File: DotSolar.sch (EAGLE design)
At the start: 19 parts, among them IC2 SI1145, Q1 BSH203, U1 ISL29125

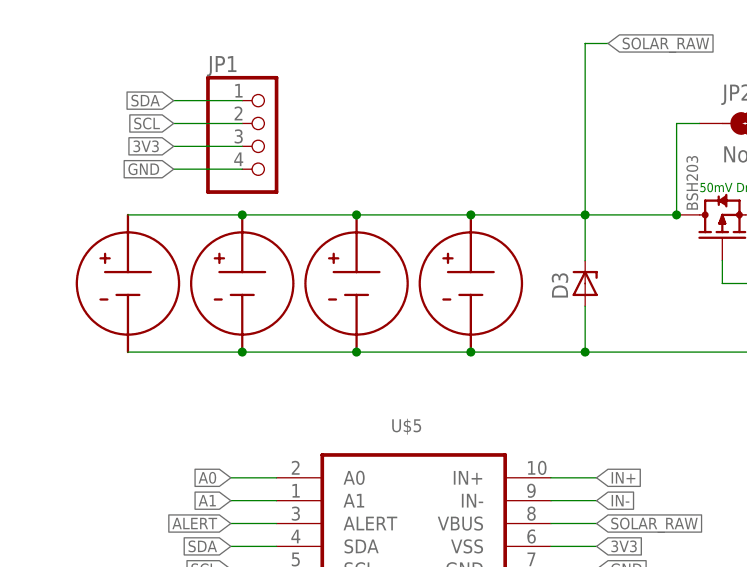
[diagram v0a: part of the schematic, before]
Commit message: Update with exdended solar pad design
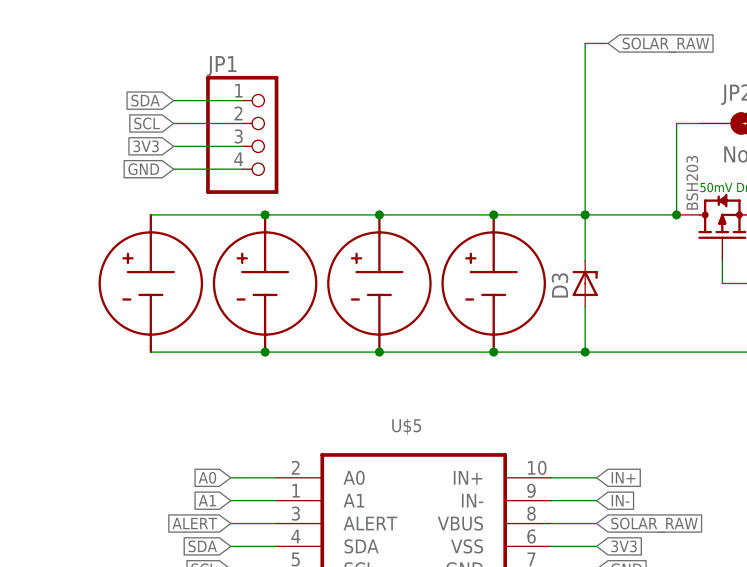
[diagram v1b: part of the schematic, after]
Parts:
- removed U$4: KXOB22-01X8F, IXYS_Solar_cells:KXOB22-01X8F
- added U$6: KXOB22-01X8F_EXTENDED_PADS, IXYS_Solar_cells:KXOB22-01X8F_EXTENDED_PADS
- U$1, U$2, U$3: value KXOB22-01X8F -> KXOB22-01X8F_EXTENDED_PADS; device IXYS_Solar_cells:KXOB22-01X8F -> IXYS_Solar_cells:KXOB22-01X8F_EXTENDED_PADS
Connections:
- net GND: now also U$6.P$1; no longer U$4.P$1
- net SOLAR_RAW: now also U$6.P$2; no longer U$4.P$2
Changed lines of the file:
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@@
 <parts>
 <part name="LOGO1" library="Particle-Devices" deviceset="OSHW-LOGO" device="S"/>
-<part name="U$1" library="IXYS_Solar_cells" deviceset="KXOB22-01X8F" device=""/>
-<part name="U$2" library="IXYS_Solar_cells" deviceset="KXOB22-01X8F" device=""/>
-<part name="U$3" library="IXYS_Solar_cells" deviceset="KXOB22-01X8F" device=""/>
-<part name="U$4" library="IXYS_Solar_cells" deviceset="KXOB22-01X8F" device=""/>
 <part name="SJ2" library="SparkFun" deviceset="SOLDERJUMPER_2WAY" device="PASTE2&amp;3"/>
 <part name="SJ3" library="SparkFun" deviceset="SOLDERJUMPER_2WAY" device="PASTE2&amp;3"/>
@@
 <part name="D1" library="PP_Passives" deviceset="DIODE" device="_B130-13-F"/>
 <part name="JP2" library="SparkFun-Jumpers" deviceset="JUMPER-SMT_2_NO" device="_SILK" value="NoBattery, only Capacitor"/>
+<part name="U$6" library="IXYS_Solar_cells" deviceset="KXOB22-01X8F_EXTENDED_PADS" device=""/>
+<part name="U$1" library="IXYS_Solar_cells" deviceset="KXOB22-01X8F_EXTENDED_PADS" device=""/>
+<part name="U$2" library="IXYS_Solar_cells" deviceset="KXOB22-01X8F_EXTENDED_PADS" device=""/>
+<part name="U$3" library="IXYS_Solar_cells" deviceset="KXOB22-01X8F_EXTENDED_PADS" device=""/>
 </parts>
 <sheets>
@@
 <instances>
 <instance part="LOGO1" gate="G$1" x="27.94" y="96.52"/>
-<instance part="U$1" gate="G$1" x="22.86" y="55.88"/>
-<instance part="U$2" gate="G$1" x="35.56" y="55.88"/>
-<instance part="U$3" gate="G$1" x="48.26" y="55.88"/>
-<instance part="U$4" gate="G$1" x="60.96" y="55.88"/>
 <instance part="SJ2" gate="G$1" x="22.86" y="-10.16" rot="R180"/>
 <instance part="SJ3" gate="G$1" x="53.34" y="-10.16" rot="R180"/>
@@
 <instance part="D1" gate="G$1" x="96.52" y="63.5"/>
 <instance part="JP2" gate="G$1" x="91.44" y="73.66"/>
+<instance part="U$6" gate="G$1" x="25.4" y="55.88"/>
+<instance part="U$1" gate="G$1" x="38.1" y="55.88"/>
+<instance part="U$2" gate="G$1" x="50.8" y="55.88"/>
+<instance part="U$3" gate="G$1" x="63.5" y="55.88"/>
 </instances>
 <busses>
@@
 <net name="SOLAR_RAW" class="0">
 <segment>
+<pinref part="U$5" gate="G$1" pin="VBUS"/>
+<wire x1="69.85" y1="29.21" x2="74.93" y2="29.21" width="0.1524" layer="91"/>
+<label x="74.93" y="29.21" size="1.27" layer="95" xref="yes"/>
+</segment>
+<segment>
 <wire x1="73.66" y1="58.42" x2="73.66" y2="63.5" width="0.1524" layer="91"/>
-<wire x1="73.66" y1="63.5" x2="60.96" y2="63.5" width="0.1524" layer="91"/>
-<wire x1="60.96" y1="63.5" x2="48.26" y2="63.5" width="0.1524" layer="91"/>
-<wire x1="48.26" y1="63.5" x2="35.56" y2="63.5" width="0.1524" layer="91"/>
-<wire x1="35.56" y1="63.5" x2="22.86" y2="63.5" width="0.1524" layer="91"/>
+<wire x1="73.66" y1="63.5" x2="63.5" y2="63.5" width="0.1524" layer="91"/>
 <junction x="73.66" y="63.5"/>
+<wire x1="63.5" y1="63.5" x2="50.8" y2="63.5" width="0.1524" layer="91"/>
+<wire x1="50.8" y1="63.5" x2="38.1" y2="63.5" width="0.1524" layer="91"/>
+<wire x1="38.1" y1="63.5" x2="25.4" y2="63.5" width="0.1524" layer="91"/>
 <wire x1="83.82" y1="63.5" x2="73.66" y2="63.5" width="0.1524" layer="91"/>
-<pinref part="U$1" gate="G$1" pin="P$2"/>
-<pinref part="U$2" gate="G$1" pin="P$2"/>
-<junction x="35.56" y="63.5"/>
-<pinref part="U$3" gate="G$1" pin="P$2"/>
-<junction x="48.26" y="63.5"/>
-<pinref part="U$4" gate="G$1" pin="P$2"/>
-<junction x="60.96" y="63.5"/>
 <pinref part="D3" gate="G$1" pin="C"/>
 <pinref part="Q1" gate="Q" pin="D"/>
@@
 <wire x1="83.82" y1="73.66" x2="83.82" y2="63.5" width="0.1524" layer="91"/>
 <junction x="83.82" y="63.5"/>
-</segment>
-<segment>
-<pinref part="U$5" gate="G$1" pin="VBUS"/>
-<wire x1="69.85" y1="29.21" x2="74.93" y2="29.21" width="0.1524" layer="91"/>
-<label x="74.93" y="29.21" size="1.27" layer="95" xref="yes"/>
+<pinref part="U$6" gate="G$1" pin="P$2"/>
+<pinref part="U$1" gate="G$1" pin="P$2"/>
+<junction x="38.1" y="63.5"/>
+<pinref part="U$2" gate="G$1" pin="P$2"/>
+<junction x="50.8" y="63.5"/>
+<pinref part="U$3" gate="G$1" pin="P$2"/>
+<junction x="63.5" y="63.5"/>
 </segment>
 </net>
@@
 <label x="27.94" y="68.58" size="1.27" layer="95" rot="R180" xref="yes"/>
 <pinref part="JP1" gate="A" pin="4"/>
-</segment>
-<segment>
-<wire x1="73.66" y1="53.34" x2="73.66" y2="48.26" width="0.1524" layer="91"/>
-<wire x1="22.86" y1="48.26" x2="35.56" y2="48.26" width="0.1524" layer="91"/>
-<wire x1="35.56" y1="48.26" x2="48.26" y2="48.26" width="0.1524" layer="91"/>
-<wire x1="48.26" y1="48.26" x2="60.96" y2="48.26" width="0.1524" layer="91"/>
-<wire x1="60.96" y1="48.26" x2="73.66" y2="48.26" width="0.1524" layer="91"/>
-<wire x1="73.66" y1="48.26" x2="102.87" y2="48.26" width="0.1524" layer="91"/>
-<junction x="73.66" y="48.26"/>
-<label x="102.87" y="48.26" size="1.27" layer="95" xref="yes"/>
-<pinref part="U$1" gate="G$1" pin="P$1"/>
-<pinref part="U$2" gate="G$1" pin="P$1"/>
-<junction x="35.56" y="48.26"/>
-<pinref part="U$3" gate="G$1" pin="P$1"/>
-<junction x="48.26" y="48.26"/>
-<pinref part="U$4" gate="G$1" pin="P$1"/>
-<junction x="60.96" y="48.26"/>
-<pinref part="D3" gate="G$1" pin="A"/>
 </segment>
 <segment>
@@
 <label x="74.93" y="24.13" size="1.27" layer="95" xref="yes"/>
 </segment>
+<segment>
+<wire x1="73.66" y1="53.34" x2="73.66" y2="48.26" width="0.1524" layer="91"/>
+<wire x1="25.4" y1="48.26" x2="38.1" y2="48.26" width="0.1524" layer="91"/>
+<wire x1="38.1" y1="48.26" x2="50.8" y2="48.26" width="0.1524" layer="91"/>
+<wire x1="50.8" y1="48.26" x2="63.5" y2="48.26" width="0.1524" layer="91"/>
+<wire x1="63.5" y1="48.26" x2="73.66" y2="48.26" width="0.1524" layer="91"/>
+<wire x1="73.66" y1="48.26" x2="102.87" y2="48.26" width="0.1524" layer="91"/>
+<junction x="73.66" y="48.26"/>
+<label x="102.87" y="48.26" size="1.27" layer="95" xref="yes"/>
+<pinref part="D3" gate="G$1" pin="A"/>
+<pinref part="U$6" gate="G$1" pin="P$1"/>
+<pinref part="U$1" gate="G$1" pin="P$1"/>
+<junction x="38.1" y="48.26"/>
+<pinref part="U$2" gate="G$1" pin="P$1"/>
+<junction x="50.8" y="48.26"/>
+<pinref part="U$3" gate="G$1" pin="P$1"/>
+<junction x="63.5" y="48.26"/>
+</segment>
 </net>

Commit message: Add C1(10uF) and C2(1uF)
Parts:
- added C1: 10uF, rcl:C-EUC0603
- added C2: 0.1uF, rcl:C-EUC0603
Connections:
- net 3V3: now also C1.1, C2.1
- net GND: now also C1.2, C2.2
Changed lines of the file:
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@@
 <part name="U$2" library="IXYS_Solar_cells" deviceset="KXOB22-01X8F_EXTENDED_PADS" device=""/>
 <part name="U$3" library="IXYS_Solar_cells" deviceset="KXOB22-01X8F_EXTENDED_PADS" device=""/>
+<part name="C1" library="rcl" deviceset="C-EU" device="C0603" value="10uF"/>
+<part name="C2" library="rcl" deviceset="C-EU" device="C0603" value="0.1uF"/>
 </parts>
 <sheets>
@@
 <instance part="U$2" gate="G$1" x="50.8" y="55.88"/>
 <instance part="U$3" gate="G$1" x="63.5" y="55.88"/>
+<instance part="C1" gate="G$1" x="200.66" y="63.5"/>
+<instance part="C2" gate="G$1" x="210.82" y="63.5"/>
 </instances>
 <busses>
@@
 <junction x="63.5" y="48.26"/>
 </segment>
+<segment>
+<pinref part="C1" gate="G$1" pin="2"/>
+<pinref part="C2" gate="G$1" pin="2"/>
+<wire x1="200.66" y1="58.42" x2="205.74" y2="58.42" width="0.1524" layer="91"/>
+<wire x1="205.74" y1="58.42" x2="210.82" y2="58.42" width="0.1524" layer="91"/>
+<junction x="205.74" y="58.42"/>
+<wire x1="205.74" y1="58.42" x2="205.74" y2="53.34" width="0.1524" layer="91"/>
+<label x="205.74" y="53.34" size="1.27" layer="95" xref="yes"/>
+</segment>
 </net>
 <net name="3V3" class="0">
@@
 <junction x="99.06" y="63.5"/>
 </segment>
+<segment>
+<pinref part="C2" gate="G$1" pin="1"/>
+<pinref part="C1" gate="G$1" pin="1"/>
+<wire x1="210.82" y1="66.04" x2="205.74" y2="66.04" width="0.1524" layer="91"/>
+<wire x1="205.74" y1="66.04" x2="200.66" y2="66.04" width="0.1524" layer="91"/>
+<wire x1="205.74" y1="66.04" x2="205.74" y2="71.12" width="0.1524" layer="91"/>
+<junction x="205.74" y="66.04"/>
+<label x="205.74" y="71.12" size="1.27" layer="95" xref="yes"/>
+</segment>
 </net>

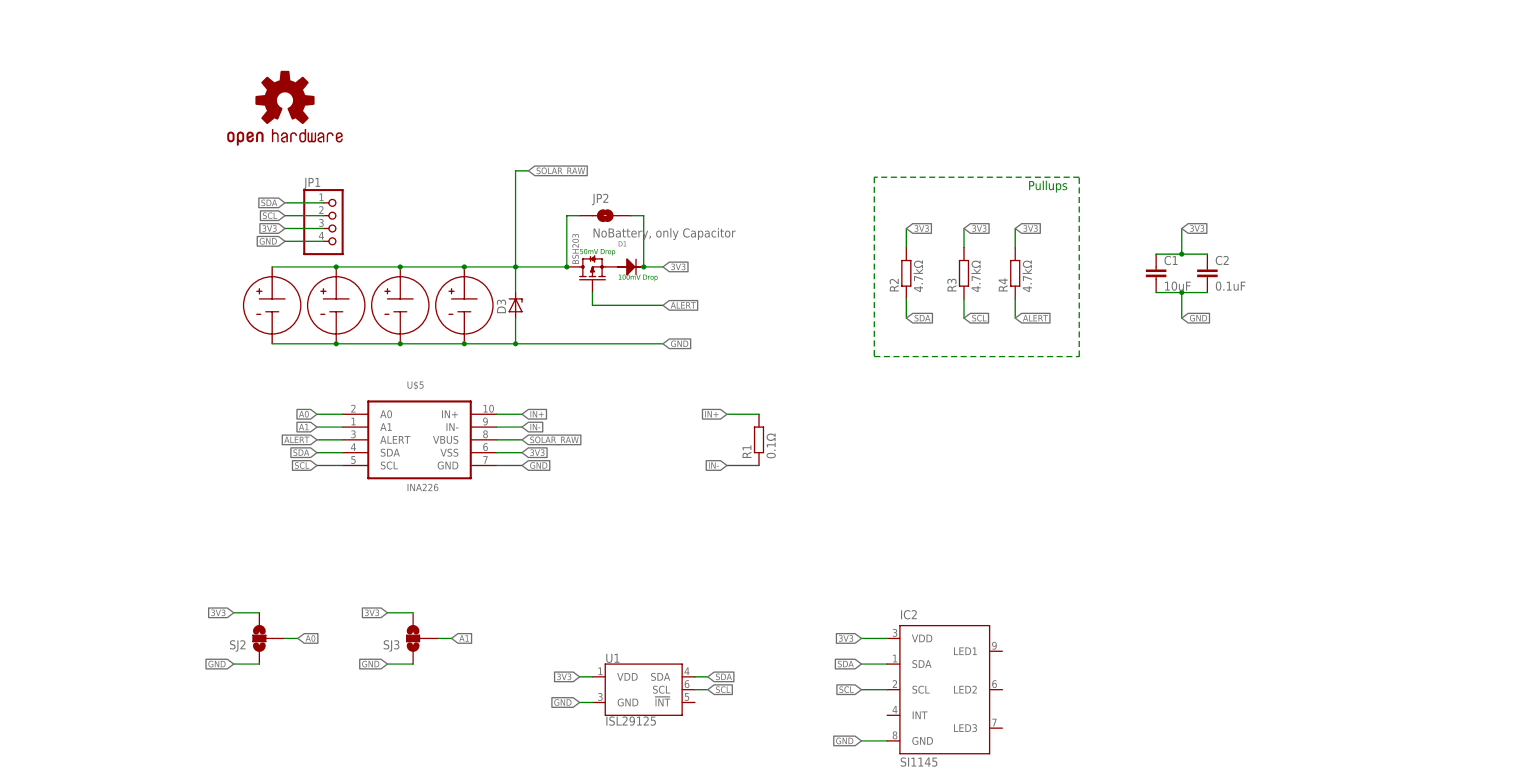
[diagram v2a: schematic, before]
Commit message: Add CAT24M01 8Mbit EEPROM
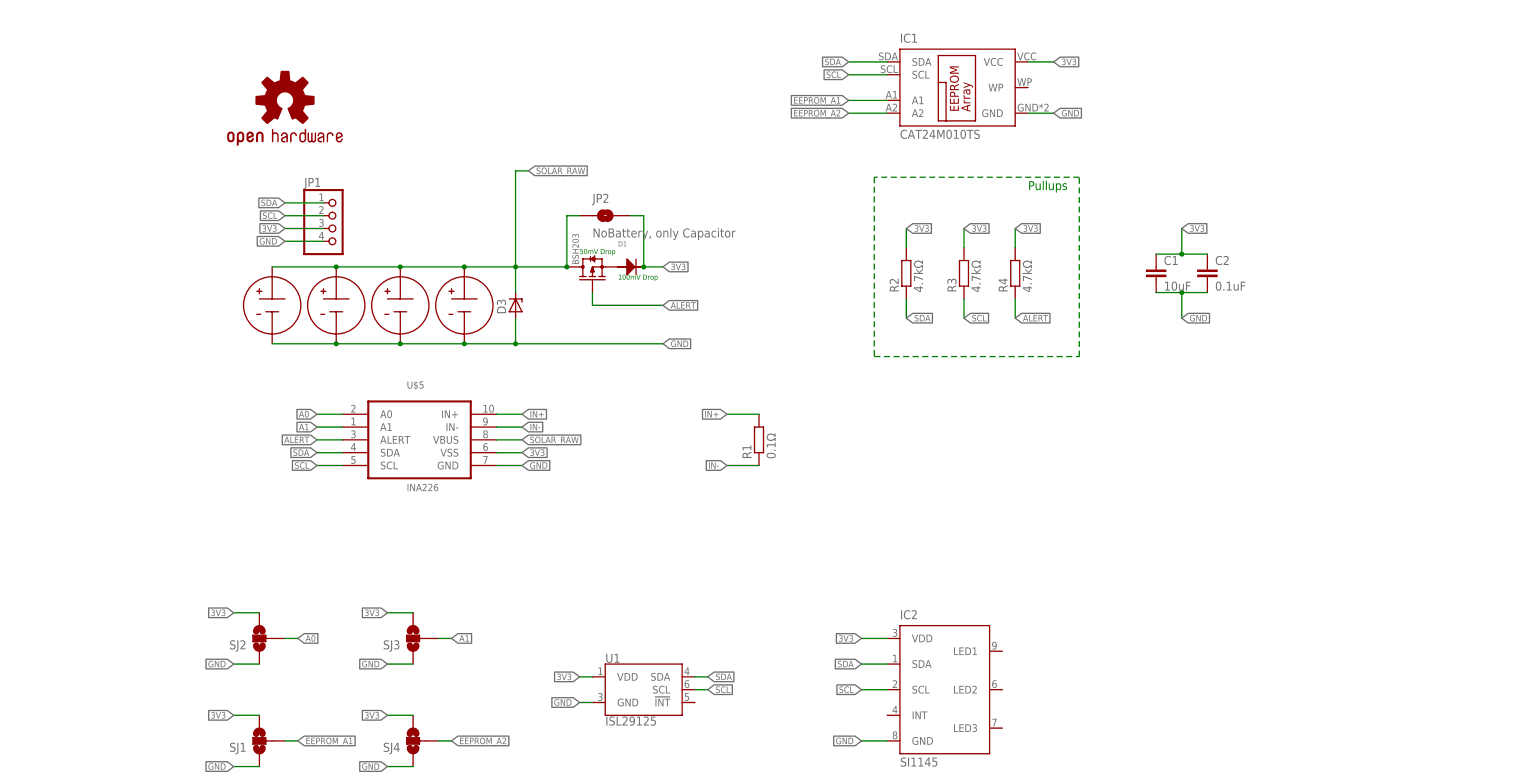
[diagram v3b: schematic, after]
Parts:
- added IC1: CAT24M010TS, CAT24M01YI:CAT24M010TS
- added SJ1, SJ4: (no value), SparkFun:SOLDERJUMPER_2WAYPASTE2&3
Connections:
- new net EEPROM_A1: IC1.A1, SJ1.2
- new net EEPROM_A2: IC1.A2, SJ4.2
- net 3V3: now also IC1.VCC, SJ1.3, SJ4.3
- net GND: now also IC1.GND, SJ1.1, SJ4.1
- net SCL: now also IC1.SCL
- net SDA: now also IC1.SDA
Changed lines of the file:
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@@
 <part name="C1" library="rcl" deviceset="C-EU" device="C0603" value="10uF"/>
 <part name="C2" library="rcl" deviceset="C-EU" device="C0603" value="0.1uF"/>
+<part name="IC1" library="CAT24M01YI" deviceset="CAT24M01" device="TS" technology="0"/>
+<part name="SJ1" library="SparkFun" deviceset="SOLDERJUMPER_2WAY" device="PASTE2&amp;3"/>
+<part name="SJ4" library="SparkFun" deviceset="SOLDERJUMPER_2WAY" device="PASTE2&amp;3"/>
 </parts>
 <sheets>
@@
 <instance part="C1" gate="G$1" x="200.66" y="63.5"/>
 <instance part="C2" gate="G$1" x="210.82" y="63.5"/>
+<instance part="IC1" gate="G$1" x="160.02" y="99.06"/>
+<instance part="SJ1" gate="G$1" x="22.86" y="-30.48" rot="R180"/>
+<instance part="SJ4" gate="G$1" x="53.34" y="-30.48" rot="R180"/>
 </instances>
 <busses>
@@
 <label x="205.74" y="53.34" size="1.27" layer="95" xref="yes"/>
 </segment>
+<segment>
+<pinref part="IC1" gate="G$1" pin="GND"/>
+<wire x1="175.26" y1="93.98" x2="180.34" y2="93.98" width="0.1524" layer="91"/>
+<label x="180.34" y="93.98" size="1.27" layer="95" xref="yes"/>
+</segment>
+<segment>
+<pinref part="SJ1" gate="G$1" pin="1"/>
+<wire x1="22.86" y1="-35.56" x2="17.78" y2="-35.56" width="0.1524" layer="91"/>
+<label x="17.78" y="-35.56" size="1.27" layer="95" rot="R180" xref="yes"/>
+</segment>
+<segment>
+<pinref part="SJ4" gate="G$1" pin="1"/>
+<wire x1="53.34" y1="-35.56" x2="48.26" y2="-35.56" width="0.1524" layer="91"/>
+<label x="48.26" y="-35.56" size="1.27" layer="95" rot="R180" xref="yes"/>
+</segment>
 </net>
 <net name="3V3" class="0">
@@
 <label x="205.74" y="71.12" size="1.27" layer="95" xref="yes"/>
 </segment>
+<segment>
+<pinref part="IC1" gate="G$1" pin="VCC"/>
+<wire x1="175.26" y1="104.14" x2="180.34" y2="104.14" width="0.1524" layer="91"/>
+<label x="180.34" y="104.14" size="1.27" layer="95" xref="yes"/>
+</segment>
+<segment>
+<pinref part="SJ1" gate="G$1" pin="3"/>
+<wire x1="22.86" y1="-25.4" x2="17.78" y2="-25.4" width="0.1524" layer="91"/>
+<label x="17.78" y="-25.4" size="1.27" layer="95" rot="R180" xref="yes"/>
+</segment>
+<segment>
+<pinref part="SJ4" gate="G$1" pin="3"/>
+<wire x1="53.34" y1="-25.4" x2="48.26" y2="-25.4" width="0.1524" layer="91"/>
+<label x="48.26" y="-25.4" size="1.27" layer="95" rot="R180" xref="yes"/>
+</segment>
 </net>
 <net name="A0" class="0">
@@
 <label x="34.29" y="26.67" size="1.27" layer="95" rot="R180" xref="yes"/>
 </segment>
+<segment>
+<pinref part="IC1" gate="G$1" pin="SDA"/>
+<wire x1="147.32" y1="104.14" x2="139.7" y2="104.14" width="0.1524" layer="91"/>
+<label x="139.7" y="104.14" size="1.27" layer="95" rot="R180" xref="yes"/>
+</segment>
 </net>
 <net name="SCL" class="0">
@@
 <wire x1="39.37" y1="24.13" x2="34.29" y2="24.13" width="0.1524" layer="91"/>
 <label x="34.29" y="24.13" size="1.27" layer="95" rot="R180" xref="yes"/>
+</segment>
+<segment>
+<pinref part="IC1" gate="G$1" pin="SCL"/>
+<wire x1="147.32" y1="101.6" x2="139.7" y2="101.6" width="0.1524" layer="91"/>
+<label x="139.7" y="101.6" size="1.27" layer="95" rot="R180" xref="yes"/>
 </segment>
 </net>
@@
 </segment>
 </net>
+<net name="EEPROM_A1" class="0">
+<segment>
+<pinref part="IC1" gate="G$1" pin="A1"/>
+<wire x1="147.32" y1="96.52" x2="139.7" y2="96.52" width="0.1524" layer="91"/>
+<label x="139.7" y="96.52" size="1.27" layer="95" rot="R180" xref="yes"/>
+</segment>
+<segment>
+<pinref part="SJ1" gate="G$1" pin="2"/>
+<wire x1="27.94" y1="-30.48" x2="30.48" y2="-30.48" width="0.1524" layer="91"/>
+<label x="30.48" y="-30.48" size="1.27" layer="95" xref="yes"/>
+</segment>
+</net>
+<net name="EEPROM_A2" class="0">
+<segment>
+<pinref part="IC1" gate="G$1" pin="A2"/>
+<wire x1="147.32" y1="93.98" x2="139.7" y2="93.98" width="0.1524" layer="91"/>
+<label x="139.7" y="93.98" size="1.27" layer="95" rot="R180" xref="yes"/>
+</segment>
+<segment>
+<pinref part="SJ4" gate="G$1" pin="2"/>
+<wire x1="58.42" y1="-30.48" x2="60.96" y2="-30.48" width="0.1524" layer="91"/>
+<label x="60.96" y="-30.48" size="1.27" layer="95" xref="yes"/>
+</segment>
+</net>

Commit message: EEPROM default address 0x52 and 0x53
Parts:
- removed SJ1: (no value), SparkFun:SOLDERJUMPER_2WAYPASTE2&3
- added JP3: JUMPER-SMT_3_1-NC_TRACE_SILK, SparkFun-Jumpers:JUMPER-SMT_3_1-NC_TRACE_SILK
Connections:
- net 3V3: now also JP3.3; no longer SJ1.3
- net EEPROM_A1: now also JP3.2; no longer SJ1.2
- net GND: now also JP3.1; no longer SJ1.1
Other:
- note added: "Address 0x52 and 0x53(upper)"
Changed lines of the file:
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@@
 <part name="C2" library="rcl" deviceset="C-EU" device="C0603" value="0.1uF"/>
 <part name="IC1" library="CAT24M01YI" deviceset="CAT24M01" device="TS" technology="0"/>
-<part name="SJ1" library="SparkFun" deviceset="SOLDERJUMPER_2WAY" device="PASTE2&amp;3"/>
 <part name="SJ4" library="SparkFun" deviceset="SOLDERJUMPER_2WAY" device="PASTE2&amp;3"/>
+<part name="JP3" library="SparkFun-Jumpers" deviceset="JUMPER-SMT_3_1-NC_TRACE" device="_SILK"/>
 </parts>
 <sheets>
@@
 <text x="93.98" y="60.96" size="1.016" layer="91">100mV Drop</text>
 <text x="175.26" y="78.74" size="1.778" layer="91">Pullups</text>
+<text x="149.86" y="111.76" size="1.778" layer="91">Address 0x52 and 0x53(upper)</text>
 </plain>
 <instances>
@@
 <instance part="C2" gate="G$1" x="210.82" y="63.5"/>
 <instance part="IC1" gate="G$1" x="160.02" y="99.06"/>
-<instance part="SJ1" gate="G$1" x="22.86" y="-30.48" rot="R180"/>
 <instance part="SJ4" gate="G$1" x="53.34" y="-30.48" rot="R180"/>
+<instance part="JP3" gate="G$1" x="22.86" y="-30.48" rot="R180"/>
 </instances>
 <busses>
@@
 </segment>
 <segment>
-<pinref part="SJ1" gate="G$1" pin="1"/>
 <wire x1="22.86" y1="-35.56" x2="17.78" y2="-35.56" width="0.1524" layer="91"/>
 <label x="17.78" y="-35.56" size="1.27" layer="95" rot="R180" xref="yes"/>
+<pinref part="JP3" gate="G$1" pin="1"/>
 </segment>
 <segment>
@@
 </segment>
 <segment>
-<pinref part="SJ1" gate="G$1" pin="3"/>
 <wire x1="22.86" y1="-25.4" x2="17.78" y2="-25.4" width="0.1524" layer="91"/>
 <label x="17.78" y="-25.4" size="1.27" layer="95" rot="R180" xref="yes"/>
+<pinref part="JP3" gate="G$1" pin="3"/>
 </segment>
 <segment>
@@
 </segment>
 <segment>
-<pinref part="SJ1" gate="G$1" pin="2"/>
 <wire x1="27.94" y1="-30.48" x2="30.48" y2="-30.48" width="0.1524" layer="91"/>
 <label x="30.48" y="-30.48" size="1.27" layer="95" xref="yes"/>
-</segment>
-</net>
+<pinref part="JP3" gate="G$1" pin="2"/>
+</segment>
+</net>
